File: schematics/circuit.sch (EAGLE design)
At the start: 19 parts, among them X1 87758-1816

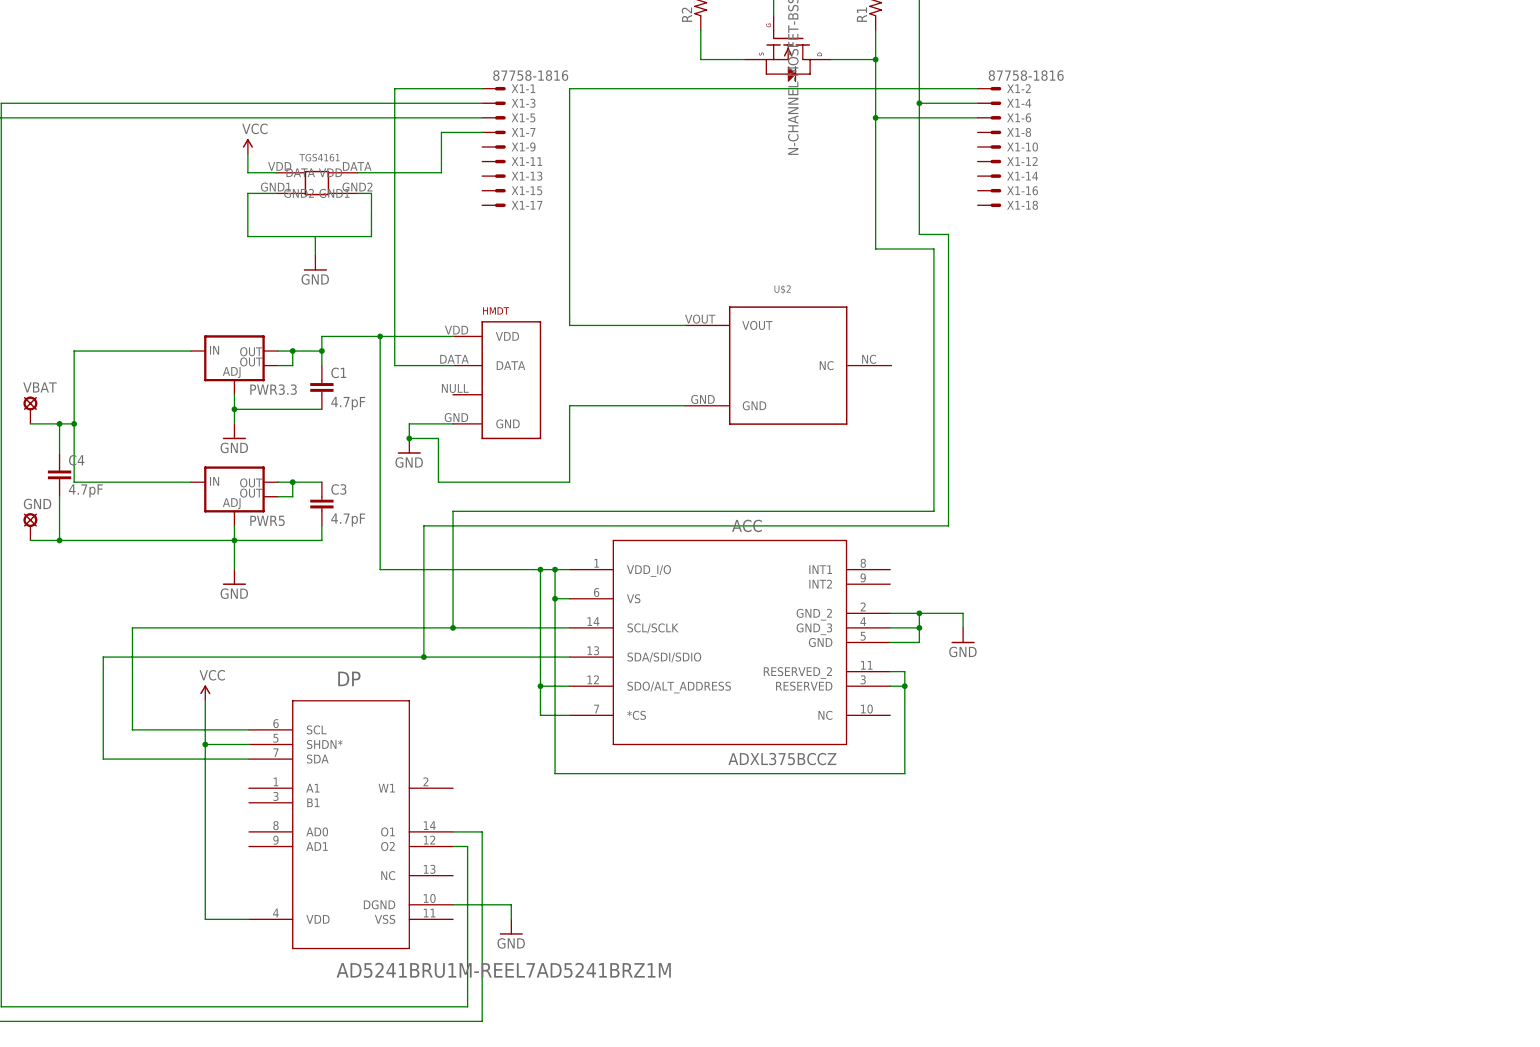
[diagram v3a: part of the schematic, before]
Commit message: В эл.схему добавлен блок переключения стержней
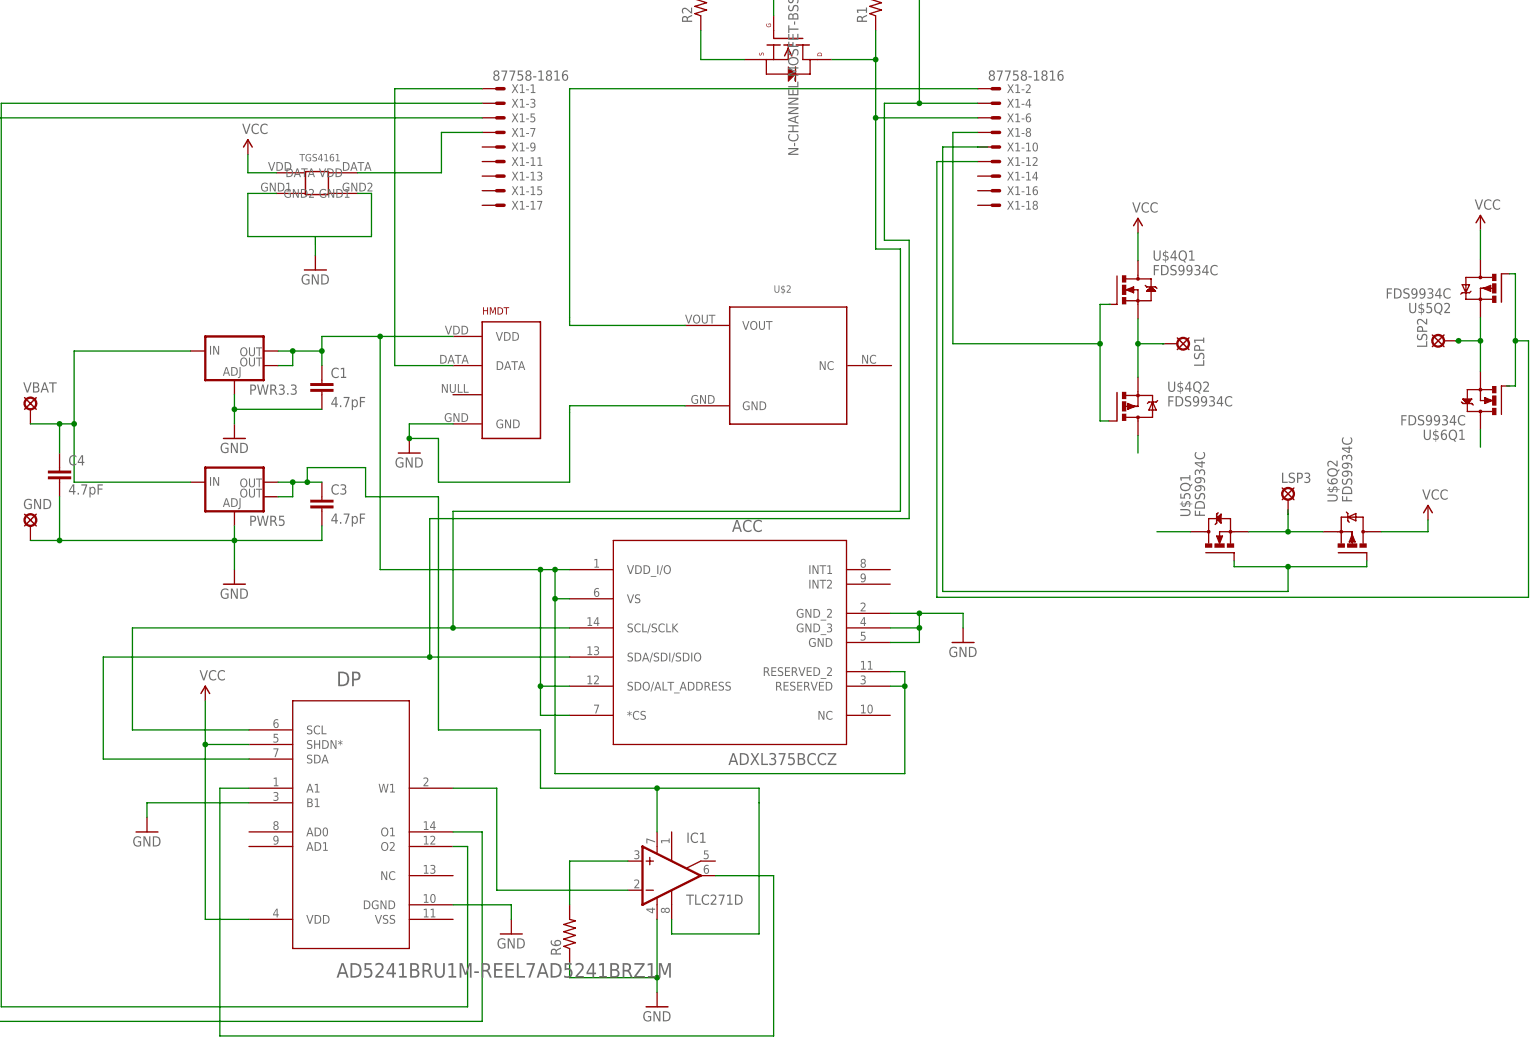
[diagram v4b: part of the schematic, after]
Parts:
- added IC1: TLC271D, linear:TLC271D
- added LSP1, LSP2, LSP3: LSP10, solpad:LSP10
- added R6: (no value), SparkFun-Passives:RESISTOR0402-RES
- added U$4, U$5, U$6: FDS9934C, bt_motordriver:FDS9934C
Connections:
- new net N$11: U$4Q2.G, X1-8.S
- new net N$12: LSP1.MP, U$4Q1.S, U$4Q2.S
- new net N$13: U$5Q2.G, X1-12.S
- new net N$14: LSP2.MP, U$5Q2.S, U$6Q1.S
- new net N$15: U$5Q1.D
- new net N$16: LSP3.MP, U$5Q1.S, U$6Q2.S
- new net N$17: U$5Q1.G, U$6Q2.G, X1-10.S
- new net N$18: U$4Q2.D
- new net N$19: U$6Q1.D
- new net N$6: DP.A1, IC1.OUT
- new net N$7: IC1.+IN, R6.2
- new net N$8: DP.W1, IC1.-IN
- new net N$9: IC1.OPT
- new net VCC: U$4Q1.D, U$5Q2.D, U$6Q2.D
- net 5V: now also IC1.V+
- net GND: now also DP.B1, IC1.V-, R6.1

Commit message: Исправил ошибки на схеме и переосмыслил её
Добавил библиотеку с коннекторами (с разъемом для SD карты)
Добавил библиотеку с датчиком влажности DHT022

Добавил в библотеку elements
GPS модуль KL3333
Комплиментарную mosfet пару AO4606
N-mosfet NTR4501N
GPS антенну A25-.....
Переосмыслил корпус для AD5241

в datchiki
Перенес SK25-F из elements (к остальным датчикам)
Исправил корпус для OPT3001 и исправил сетку в его символе
Исправил корпус TGS46... (переименовал и правильно разместил контакты)  и сетку в символе (добавил схему внутренностей на символ)
Исправил корпус O2-A2 (перевернул и правильно разместил контакты) и сетку в символе
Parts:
- removed DP: AD5241BRU1M-REEL7AD5241BRZ1M, elements:AD5241BRU1M-REEL7AD5241BRZ1M
- removed IC1: TLC271D, linear:TLC271D
- removed LSP1, LSP2, LSP3: LSP10, solpad:LSP10
- removed TGS4161: TGS4161, opt3001:TGS4161
- removed U$3: N-CHANNEL-MOSFET-BSS138, GeekAmmo:N-CHANNEL-MOSFET-BSS138
- removed U$5, U$6: FDS9934C, bt_motordriver:FDS9934C
- added IC2: TLC271D, linear:TLC271D
- added LED1, LED2, LED3, LED4, LED5, LED6: (no value), led:LEDSML0805
- added PROBE_1, PROBE_2, PROBE_3: (no value), wirepad:2,54/0,8
- added Q1, Q2: (no value), transistors:2N7002_SOT23
- added R11, R12, R5, R7, R9: 10, SparkFun-Resistors:RESISTOR0402
- added R13, R14: (no value), SparkFun-Passives:RESISTOR0402-RES
- added R8: 10k, SparkFun-Passives:RESISTOR0402-RES
- added U1: AD5241BRU1M-REEL7AD5241BRZ1M, elements:AD5241BRU1M-REEL7AD5241BRZ1M
- R1, R2, R3, R4: value (none) -> 10k
- R6: value (none) -> 10; device SparkFun-Passives:RESISTOR0402-RES -> SparkFun-Resistors:RESISTOR0402
- U$1: value N-CHANNEL-MOSFET-BSS138 -> AO4606; device GeekAmmo:N-CHANNEL-MOSFET-BSS138 -> elements:AO4606
- U$2: value O2-A2 -> AO4606; device opt3001:O2-A2 -> elements:AO4606
- U$4: value FDS9934C -> AO4606; device bt_motordriver:FDS9934C -> elements:AO4606
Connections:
- removed net N$15: U$5Q1.D
- removed net N$18: U$4Q2.D
- removed net N$19: U$6Q1.D
- removed net SCL5V: ACC.SCL/SCLK, DP.SCL, R1.1, U$3.D, X1-6.S
- removed net SDA5V: ACC.SDA/SDI/SDIO, DP.SDA, R4.1, U$1.D, X1-4.S
- removed net VCC: U$4Q1.D, U$5Q2.D, U$6Q2.D
- new net N$20: IC2.OUT, U1.A1, X1-9.S
- new net N$21: PROBE_3.P, U$2Q1.D, U$2Q2.D
- new net N$26: IC2.-IN, U1.W1
- new net N$28: R14.2, U1.O1, U1.SHDN*
- new net SCL_3.3V: ACC.SCL/SCLK, Q2.S, R2.1
- new net SCL_5V: Q2.D, R1.1, U1.SCL, X1-6.S
- new net SDA_3.3V: ACC.SDA/SDI/SDIO, Q1.S, R3.1
- new net SDA_5V: Q1.D, R4.1, U1.SDA, X1-4.S
- net 3.3V: now also Q1.G, Q2.G, R8.2; no longer U$1.G, U$3.G
- net 5V: now also IC2.ON1, IC2.OPT, U$1Q1.S, U$2Q1.S, U$4Q1.S, U1.AD0, U1.AD1, U1.VDD, U1.VSS; no longer DP.SHDN*, DP.VDD, IC1.V+
- net GND: now also IC2.V-, LED1.C, LED2.C, LED3.C, LED4.C, LED5.C, LED6.C, R13.1, R14.1, U1.DGND; no longer DP.B1, DP.DGND, IC1.V-, R6.1
- net N$1: now also LED4.A, R12.1; no longer X1-2.S
- net N$10: now also LED3.A, R6.1; no longer DP.O1, X1-5.S
- net N$11: now also R5.2, U$1Q1.G, X1-12.S; no longer U$4Q2.G, X1-8.S
- net N$12: now also LED5.A, R7.1; no longer LSP1.MP, U$4Q1.S, U$4Q2.S
- net N$13: now also R7.2, U$2Q1.G, X1-16.S; no longer U$5Q2.G, X1-12.S
- net N$14: now also LED6.A, R9.1; no longer LSP2.MP, U$5Q2.S, U$6Q1.S
- net N$16: now also PROBE_1.P, U$4Q1.D, U$4Q2.D; no longer LSP3.MP, U$5Q1.S, U$6Q2.S
- net N$17: now also R6.2, U$1Q2.G, X1-14.S; no longer U$5Q1.G, U$6Q2.G, X1-10.S
- net N$2: now also PROBE_2.P, U$1Q1.D, U$1Q2.D; no longer HMDT.DATA, X1-1.S
- net N$3: now also HMDT.DATA, R8.1, X1-2.S; no longer R3.1, U$1.S
- net N$4: now also LED1.A, R11.1; no longer DP.O2, X1-3.S
- net N$5: now also IC2.+IN, R13.2, U$1Q2.S, U$2Q2.S, U$4Q2.S; no longer R2.1, U$3.S
- net N$6: now also R11.2, U$4Q2.G, X1-10.S; no longer DP.A1, IC1.OUT
- net N$7: now also R12.2, U$4Q1.G, X1-8.S; no longer IC1.+IN, R6.2
- net N$8: now also LED2.A, R5.1; no longer DP.W1, IC1.-IN
- net N$9: now also R9.2, U$2Q2.G, X1-18.S; no longer IC1.OPT
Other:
- note removed: "3.3V"
- note removed: "5V"
- note removed: "SCL"
- note removed: "SDA"
- moved on the sheet: ACC, C3, HMDT, R1, R2, R3, R4, R6, X1-10, X1-12, X1-14, X1-16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

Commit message: почти закончили схему (кроме пережигателей, термисторов, выключателей и флешки) + начала разводить плату
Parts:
- added IC1: TLC271D, linear:TLC271D
- added R16, R18, R19: 10, SparkFun-Resistors:RESISTOR0402
- added R17: (no value), SparkFun-Passives:RESISTOR0402-RES
- added U$3: OPT3001, datchiki:OPT3001
- added U$5: TGS4161, datchiki:TGS4161
- added U$6: O2-A2, datchiki:O2-A2
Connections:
- new net N$19: R16.1, U$3.INT
- new net N$22: IC1.+IN, U$5.SENS+
- new net N$24: IC1.OUT, R18.2, X1-17.S
- net 3.3V: now also R16.2, U$3.VDD
- net 5V: now also IC1.-IN, IC1.ON1, R17.2, R18.1, R19.2, U$5.HEAT+, U$6.VOUT
- net GND: now also IC1.V-, R17.1, R19.1, U$3.ADDR, U$3.GND, U$5.SENS-, U$6.GND
- net SCL_3.3V: now also U$3.SCL
- net SDA_3.3V: now also U$3.SDA
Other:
- moved on the sheet: HMDT, R8, X1-17, X1-2

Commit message: В схему добавлены пережигатели и выключатель + обновлена плата + начата работа с отдельной платой для gps
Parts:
- removed X1: 87758-1816, con-molex:87758-1816
- added PROBE_10, PROBE_11, PROBE_12, PROBE_13, PROBE_14, PROBE_5, PROBE_6, PROBE_7, PROBE_8, PROBE_9: (no value), wirepad:2,54/0,8
- added Q3, Q4, Q5, Q6, Q7: (no value), elements:NTR4501N
- added U$9: SS-8, elements:SS-8
- added X2, X3, X4, X5, X8, X9: 87758-0216, con-molex:87758-0216
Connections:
- new net N$18: PROBE_5.P, Q3.D
- new net N$23: PROBE_8.P, Q4.D
- new net N$25: PROBE_12.P
- new net N$27: PROBE_7.P, Q5.D
- new net N$29: PROBE_11.P, Q6.D
- new net N$30: PROBE_13.P, Q7.D
- new net N$31: PROBE_10.P
- new net N$32: PROBE_6.P
- new net N$33: U$9.P2, VBAT.MP
- new net N$34: PROBE_9.P
- net GND: now also Q3.S, Q4.S, Q5.S, Q6.S, Q7.S
- net N$11: now also X9-1.S; no longer X1-12.S
- net N$13: now also X5-1.S; no longer X1-16.S
- net N$17: now also X9-2.S; no longer X1-14.S
- net N$20: now also X3-1.S; no longer X1-9.S
- net N$24: now also X3-2.S; no longer X1-17.S
- net N$3: now also X8-1.S; no longer X1-2.S
- net N$6: now also X4-2.S; no longer X1-10.S
- net N$7: now also X4-1.S; no longer X1-8.S
- net N$9: now also X5-2.S; no longer X1-18.S
- net SCL_5V: now also X2-1.S; no longer X1-6.S
- net SDA_5V: now also X2-2.S; no longer X1-4.S
- net VBAT: now also PROBE_14.P, U$9.COM; no longer VBAT.MP
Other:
- moved on the sheet: VBAT

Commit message: Исправил пару мелких ошибок на схеме. Вынес регуляторы напряжения из спаркфановской библиотеки в нашу - elements и правильно объединил им выводы. Исправил символ для TGS* датчика CO2. Все элементы обновил на схеме
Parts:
- removed PWR3.3, PWR5: (no value), SparkFun-PowerIC:V_REG_LM1117SOT223
- added U2: (no value), elements:TLV1117-33
- added U3: (no value), elements:LD1117S50
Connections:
- removed net N$31: PROBE_10.P
- removed net N$32: PROBE_6.P
- removed net N$34: PROBE_9.P
- net 3.3V: now also U2.OUT; no longer PWR3.3.OUT, PWR3.3.OUT@1
- net 5V: now also U3.OUT; no longer PWR5.OUT, PWR5.OUT@1
- net GND: now also U$5.HEAT-, U2.ADJ, U3.ADJ; no longer PWR3.3.ADJ, PWR5.ADJ
- net VBAT: now also PROBE_10.P, PROBE_6.P, PROBE_9.P, U2.IN, U3.IN; no longer PWR3.3.IN, PWR5.IN
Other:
- moved on the sheet: PROBE_10, PROBE_11, PROBE_12, PROBE_13, PROBE_14, PROBE_5, PROBE_6, PROBE_7, PROBE_8, PROBE_9, Q3, Q4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
